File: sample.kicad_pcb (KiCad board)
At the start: 2 copper layers, 30 parts, among them CN10 Conn_02x17_Odd_Even, CN7 Conn_02x10_Odd_Even, CN8 Conn_02x08_Odd_Even, CN9 Conn_02x15_Odd_Even, U1 TJA1042T-3, U2 TJA1042T-3, U3 TJA1042T-3

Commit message: place CNs correctly (?)
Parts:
- added DeviceUART1: DE9_Plug, Connector_Dsub:DSUB-9_Female_Horizontal_P2.77x2.54mm_EdgePinOffset9.40mm, F.Cu at (86.1, 106.0)
- added R10: 0R, Resistor_SMD:R_1206_3216Metric_Pad1.30x1.75mm_HandSolder, F.Cu at (153.5, 146.7)
- added R11: 0R, Resistor_SMD:R_1206_3216Metric_Pad1.30x1.75mm_HandSolder, F.Cu at (153.5, 151.9)
- added R12: 0R, Resistor_SMD:R_1206_3216Metric_Pad1.30x1.75mm_HandSolder, F.Cu at (153.5, 157.2)
- added RoutedUART1: DE9_Plug, Connector_Dsub:DSUB-9_Male_Horizontal_P2.77x2.54mm_EdgePinOffset9.40mm, F.Cu at (86.5, 58.5)
- moved C7 84.8 mm to (133.9, 151.8)
- moved R6 84.8 mm to (126.0, 148.4)
- moved R7 84.8 mm to (139.9, 148.4)
- moved C3 84.8 mm to (133.9, 157.2)
- moved C5 84.8 mm to (133.9, 160.5)
- moved C9 84.8 mm to (120.0, 151.8)
- moved R2 84.8 mm to (139.9, 157.1)
- moved R3 84.8 mm to (139.9, 160.4)
- moved R8 84.8 mm to (139.9, 151.7)
- moved R9 84.8 mm to (126.0, 151.7)
- moved C1 84.8 mm to (133.9, 145.1)
- moved C2 84.8 mm to (133.9, 148.4)
- moved C4 84.8 mm to (120.0, 145.1)
- moved C6 84.8 mm to (120.0, 148.4)
- moved C8 84.8 mm to (133.9, 163.8)
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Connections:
- net /ZIO Connector/PE2 renamed USART10_RX
- CN10 pad 18: /ZIO Connector/PE8 -> UART7_TX
- CN10 pad 19: /ZIO Connector/PD13 -> CAN3_STB
- CN10 pad 2: /ZIO Connector/PG12 -> USART10_TX
- CN10 pad 20: /ZIO Connector/PE7 -> UART7_RX
- CN10 pad 21: /ZIO Connector/PD12 -> CAN2_STB
- CN10 pad 23: /ZIO Connector/PD11 -> CAN1_STB
- CN10 pad 29: /ZIO Connector/PA0 -> UART4_TX
- CN10 pad 32: /ZIO Connector/PB10 -> USART3_TX
- CN10 pad 34: /ZIO Connector/PB11 -> USART3_RX
- CN7 pad 1: /ZIO Connector/PC6 -> USART6_TX
- CN7 pad 11: /ZIO Connector/PC7 -> USART6_RX
- CN7 pad 20: /ZIO Connector/PB8 -> /ZIO Connector/PF3
- CN8 pad 10: /ZIO Connector/PC12 -> UART5_TX
- CN8 pad 12: /ZIO Connector/PD2 -> UART5_RX
- CN8 pad 8: /ZIO Connector/PC11 -> UART4_RX
- CN9 pad 1: /ZIO Connector/PA3 -> USART2_RX
- CN9 pad 29: /ZIO Connector/PG0 -> UART9_RX
- CN9 pad 30: /ZIO Connector/PG1 -> UART9_TX
- CN9 pad 6: /ZIO Connector/PD5 -> USART2_TX
- R1 pad 1: CAN3_STB -> Net-(U3-STB)
- R3 pad 1: CAN1_STB -> Net-(U1-STB)
- R4 pad 1: CAN2_STB -> Net-(U2-STB)
- U1 pad 8: CAN1_STB -> Net-(U1-STB)
- U2 pad 8: CAN2_STB -> Net-(U2-STB)
- U3 pad 8: CAN3_STB -> Net-(U3-STB)

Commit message: fix some placement
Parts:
- moved R3 110.0 mm to (131.9, 50.7), turned to 90 degrees
- moved R10 99.1 mm to (128.4, 50.8), turned to -90 degrees
- moved C3 98.8 mm to (120.4, 59.2), turned to 180 degrees
- moved C5 98.8 mm to (138.9, 61.8), turned to -90 degrees
- moved R5 98.3 mm to (126.9, 66.2), turned to -90 degrees
- moved C8 92.8 mm to (128.4, 71.2)
- moved R2 91.3 mm to (130.9, 66.3), turned to -90 degrees
- moved R11 72.8 mm to (130.9, 82.7), turned to -90 degrees
- moved R4 62.3 mm to (126.4, 82.7), turned to 90 degrees
- moved C9 60.6 mm to (135.4, 93.2), turned to -90 degrees
- moved U1 59.4 mm to (129.4, 58.2)
- moved JP1 58.9 mm to (138.8, 83.2)
- moved JP2 58.9 mm to (138.8, 86.5)
- moved R12 54.7 mm to (126.4, 109.7), turned to -90 degrees
- moved R9 54.5 mm to (125.4, 97.2), turned to -90 degrees
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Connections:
- CN8 pad 15: GND -> /ZIO Connector/VIN

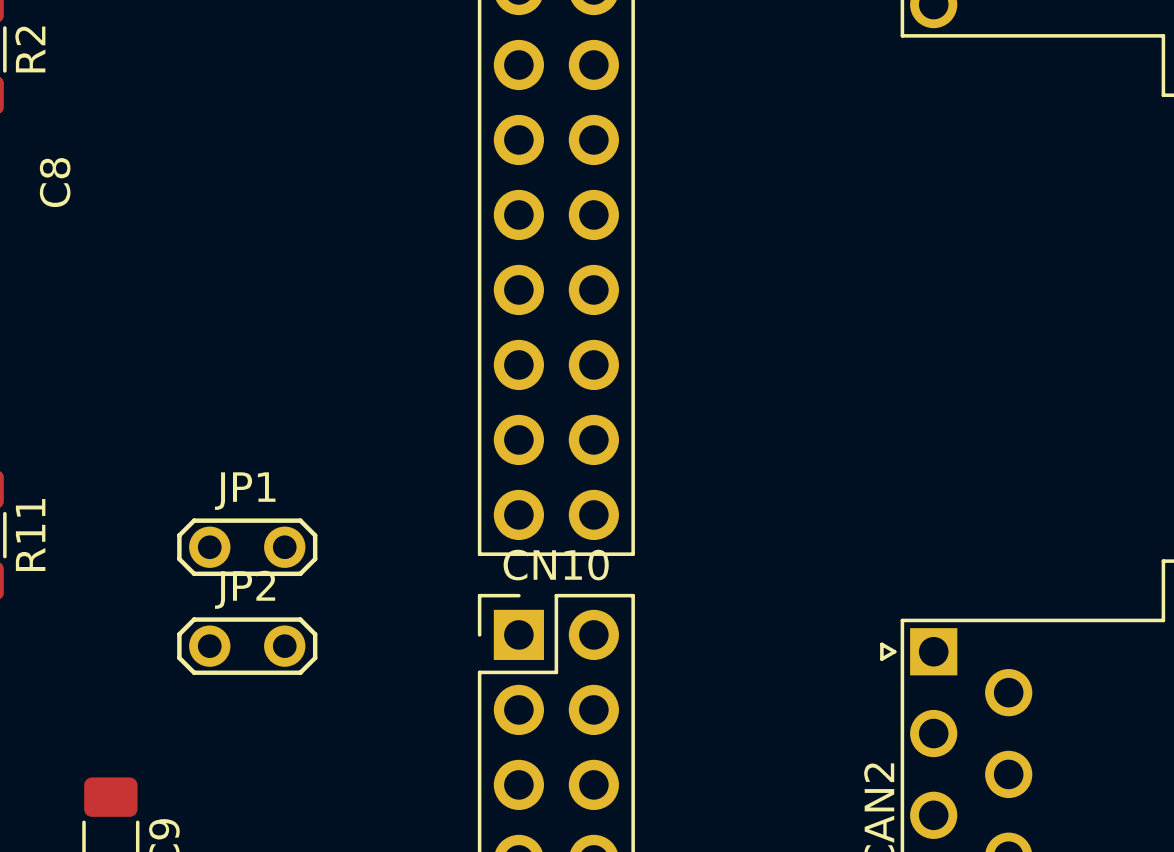
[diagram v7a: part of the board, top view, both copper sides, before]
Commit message: readdress CAN pins for better routing
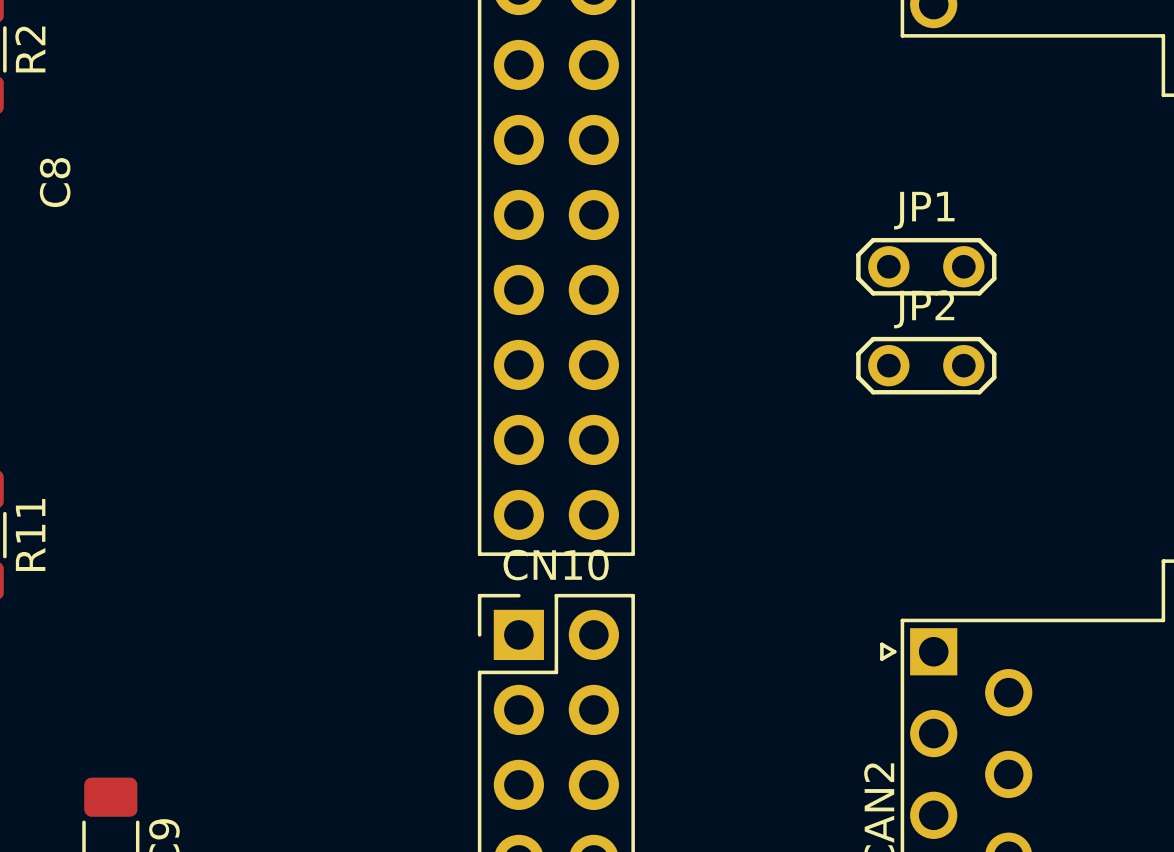
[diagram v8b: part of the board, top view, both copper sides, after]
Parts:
- moved JP1 24.9 mm to (161.8, 73.7)
- moved JP2 24.9 mm to (161.8, 77.0)
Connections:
- CN10 pad 11: CAN3_RX -> /ZIO Connector/PF6
- CN10 pad 15: /ZIO Connector/PB2 -> CAN2_STB
- CN10 pad 19: CAN3_STB -> CAN3_TX
- CN10 pad 21: CAN2_STB -> CAN3_RX
- CN10 pad 23: CAN1_STB -> CAN3_STB
- CN7 pad 13: /ZIO Connector/PB5 -> CAN2_RX
- CN7 pad 14: /ZIO Connector/PB5 -> CAN2_RX
- CN7 pad 2: /ZIO Connector/PB8 -> CAN1_RX
- CN7 pad 4: /ZIO Connector/PB9 -> CAN1_TX
- CN7 pad 7: CAN2_RX -> CAN1_STB
- CN9 pad 25: CAN1_RX -> /ZIO Connector/PD0
- CN9 pad 26: CAN3_TX -> /ZIO Connector/PF7
- CN9 pad 27: CAN1_TX -> /ZIO Connector/PD1
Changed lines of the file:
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@@
 	(net 26 "CAN3_RX")
 	(net 27 "CAN3_TX")
-	(net 28 "/ZIO Connector/PB8")
+	(net 28 "/ZIO Connector/PF7")
 	(net 29 "/ZIO Connector/PB15")
-	(net 30 "/ZIO Connector/PB5")
-	(net 31 "/ZIO Connector/PB9")
+	(net 30 "/ZIO Connector/PD1")
+	(net 31 "/ZIO Connector/PD0")
 	(net 32 "/ZIO Connector/PD14")
 	(net 33 "/ZIO Connector/PB3")
@@
 	(net 71 "/ZIO Connector/PE9")
 	(net 72 "/ZIO Connector/PE0")
-	(net 73 "/ZIO Connector/PB2")
+	(net 73 "/ZIO Connector/PF6")
 	(net 74 "/ZIO Connector/PG14")
 	(net 75 "/ZIO Connector/PE10")
@@
 		(tags "resistor handsolder")
 		(property "Reference" "R1"
-			(at 0 -1.82 270)
+			(at 0 -1.82 -90)
 			(layer "F.SilkS")
 			(effects
@@
 		)
 		(property "Value" "R"
-			(at 0 1.82 270)
+			(at 0 1.82 -90)
 			(layer "F.Fab")
 			(effects
@@
 		)
 		(fp_text user "${REFERENCE}"
-			(at 0 0 270)
+			(at 0 0 -90)
 			(layer "F.Fab")
 			(effects
@@
 			(layers "*.Cu" "*.Mask")
 			(remove_unused_layers no)
-			(net 14 "CAN1_RX")
+			(net 31 "/ZIO Connector/PD0")
 			(pinfunction "Pin_25")
 			(pintype "passive")
@@
 			(layers "*.Cu" "*.Mask")
 			(remove_unused_layers no)
-			(net 27 "CAN3_TX")
+			(net 28 "/ZIO Connector/PF7")
 			(pinfunction "Pin_26")
 			(pintype "passive")
@@
 			(layers "*.Cu" "*.Mask")
 			(remove_unused_layers no)
-			(net 13 "CAN1_TX")
+			(net 30 "/ZIO Connector/PD1")
 			(pinfunction "Pin_27")
 			(pintype "passive")
@@
 		(tags "resistor handsolder")
 		(property "Reference" "R4"
-			(at 0 -1.82 270)
+			(at 0 -1.82 -90)
 			(layer "F.SilkS")
 			(effects
@@
 		)
 		(property "Value" "R"
-			(at 0 1.82 270)
+			(at 0 1.82 -90)
 			(layer "F.Fab")
 			(effects
@@
 		)
 		(fp_text user "${REFERENCE}"
-			(at 0 0 270)
+			(at 0 0 -90)
 			(layer "F.Fab")
 			(effects
@@
 	(footprint "TestPoint:TestPoint_2Pads_Pitch2.54mm_Drill0.8mm"
 		(layer "F.Cu")
-		(at 138.75 83.15)
+		(at 161.75 73.65)
 		(descr "Test point with 2 pins, pitch 2.54mm, drill diameter 0.8mm")
 		(tags "CONN DEV")
@@
 			(layers "*.Cu" "*.Mask")
 			(remove_unused_layers no)
-			(net 28 "/ZIO Connector/PB8")
+			(net 14 "CAN1_RX")
 			(pinfunction "Pin_2")
 			(pintype "passive")
@@
 			(layers "*.Cu" "*.Mask")
 			(remove_unused_layers no)
-			(net 31 "/ZIO Connector/PB9")
+			(net 13 "CAN1_TX")
 			(pinfunction "Pin_4")
 			(pintype "passive")
@@
 			(layers "*.Cu" "*.Mask")
 			(remove_unused_layers no)
-			(net 25 "CAN2_RX")
+			(net 17 "CAN1_STB")
 			(pinfunction "Pin_7")
 			(pintype "passive")
@@
 			(layers "*.Cu" "*.Mask")
 			(remove_unused_layers no)
-			(net 30 "/ZIO Connector/PB5")
+			(net 25 "CAN2_RX")
 			(pinfunction "Pin_13")
 			(pintype "passive")
@@
 			(layers "*.Cu" "*.Mask")
 			(remove_unused_layers no)
-			(net 30 "/ZIO Connector/PB5")
+			(net 25 "CAN2_RX")
 			(pinfunction "Pin_14")
 			(pintype "passive")
@@
 	(footprint "TestPoint:TestPoint_2Pads_Pitch2.54mm_Drill0.8mm"
 		(layer "F.Cu")
-		(at 138.75 86.5)
+		(at 161.75 77)
 		(descr "Test point with 2 pins, pitch 2.54mm, drill diameter 0.8mm")
 		(tags "CONN DEV")
@@
 		(tags "capacitor handsolder")
 		(property "Reference" "C6"
-			(at 0 -1.85 360)
+			(at 0 -1.85 0)
 			(layer "F.SilkS")
 			(effects
@@
 		)
 		(fp_text user "${REFERENCE}"
-			(at 0 0 360)
+			(at 0 0 0)
 			(layer "F.Fab")
 			(effects
@@
 		(tags "resistor handsolder")
 		(property "Reference" "R3"
-			(at 0 -1.82 270)
+			(at 0 -1.82 -90)
 			(layer "F.SilkS")
 			(effects
@@
 		)
 		(property "Value" "R"
-			(at 0 1.82 270)
+			(at 0 1.82 -90)
 			(layer "F.Fab")
 			(effects
@@
 		)
 		(fp_text user "${REFERENCE}"
-			(at 0 0 270)
+			(at 0 0 -90)
 			(layer "F.Fab")
 			(effects
@@
 			(layers "*.Cu" "*.Mask")
 			(remove_unused_layers no)
-			(net 26 "CAN3_RX")
+			(net 73 "/ZIO Connector/PF6")
 			(pinfunction "Pin_11")
 			(pintype "passive")
@@
 			(layers "*.Cu" "*.Mask")
 			(remove_unused_layers no)
-			(net 73 "/ZIO Connector/PB2")
+			(net 18 "CAN2_STB")
 			(pinfunction "Pin_15")
 			(pintype "passive")
@@
 			(layers "*.Cu" "*.Mask")
 			(remove_unused_layers no)
-			(net 15 "CAN3_STB")
+			(net 27 "CAN3_TX")
 			(pinfunction "Pin_19")
 			(pintype "passive")
@@
 			(layers "*.Cu" "*.Mask")
 			(remove_unused_layers no)
-			(net 18 "CAN2_STB")
+			(net 26 "CAN3_RX")
 			(pinfunction "Pin_21")
 			(pintype "passive")
@@
 			(layers "*.Cu" "*.Mask")
 			(remove_unused_layers no)
-			(net 17 "CAN1_STB")
+			(net 15 "CAN3_STB")
 			(pinfunction "Pin_23")
 			(pintype "passive")
@@
 		)
 		(property "Value" "C"
-			(at 0 1.85 360)
+			(at 0 1.85 0)
 			(layer "F.Fab")
 			(effects
@@
 		)
 		(fp_text user "${REFERENCE}"
-			(at 0 0 360)
+			(at 0 0 0)
 			(layer "F.Fab")
 			(effects
